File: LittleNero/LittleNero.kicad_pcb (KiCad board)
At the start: 2 copper layers, 24 parts, among them J1 USB_B_Mini, SW1 SW_push, U1 ATmega32U4-AU, Y1 16MHz

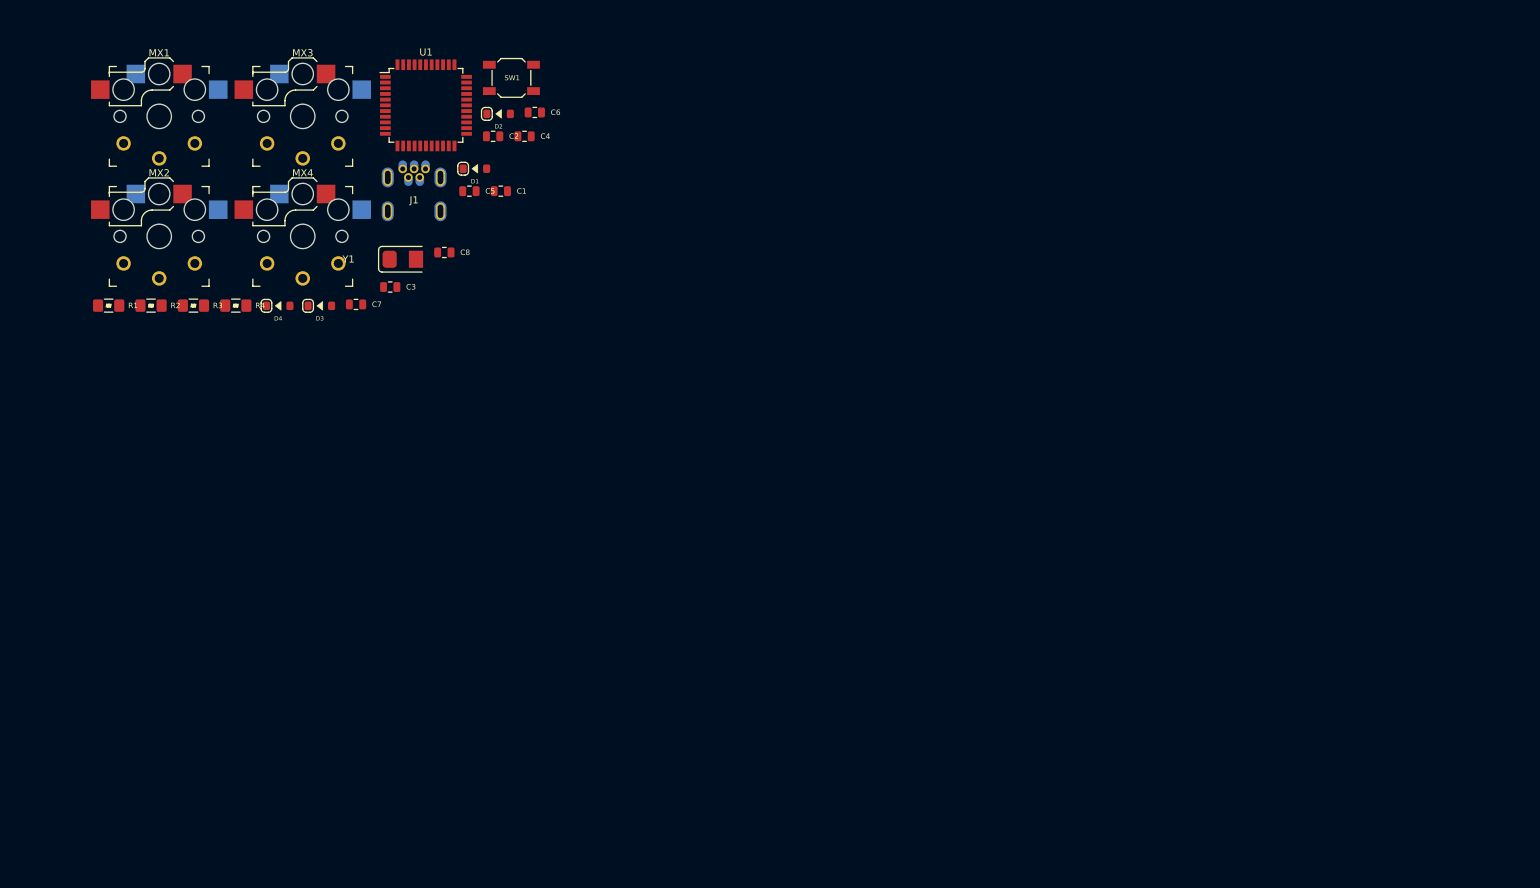
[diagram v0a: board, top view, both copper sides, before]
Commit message: updated schematic + visual pcb
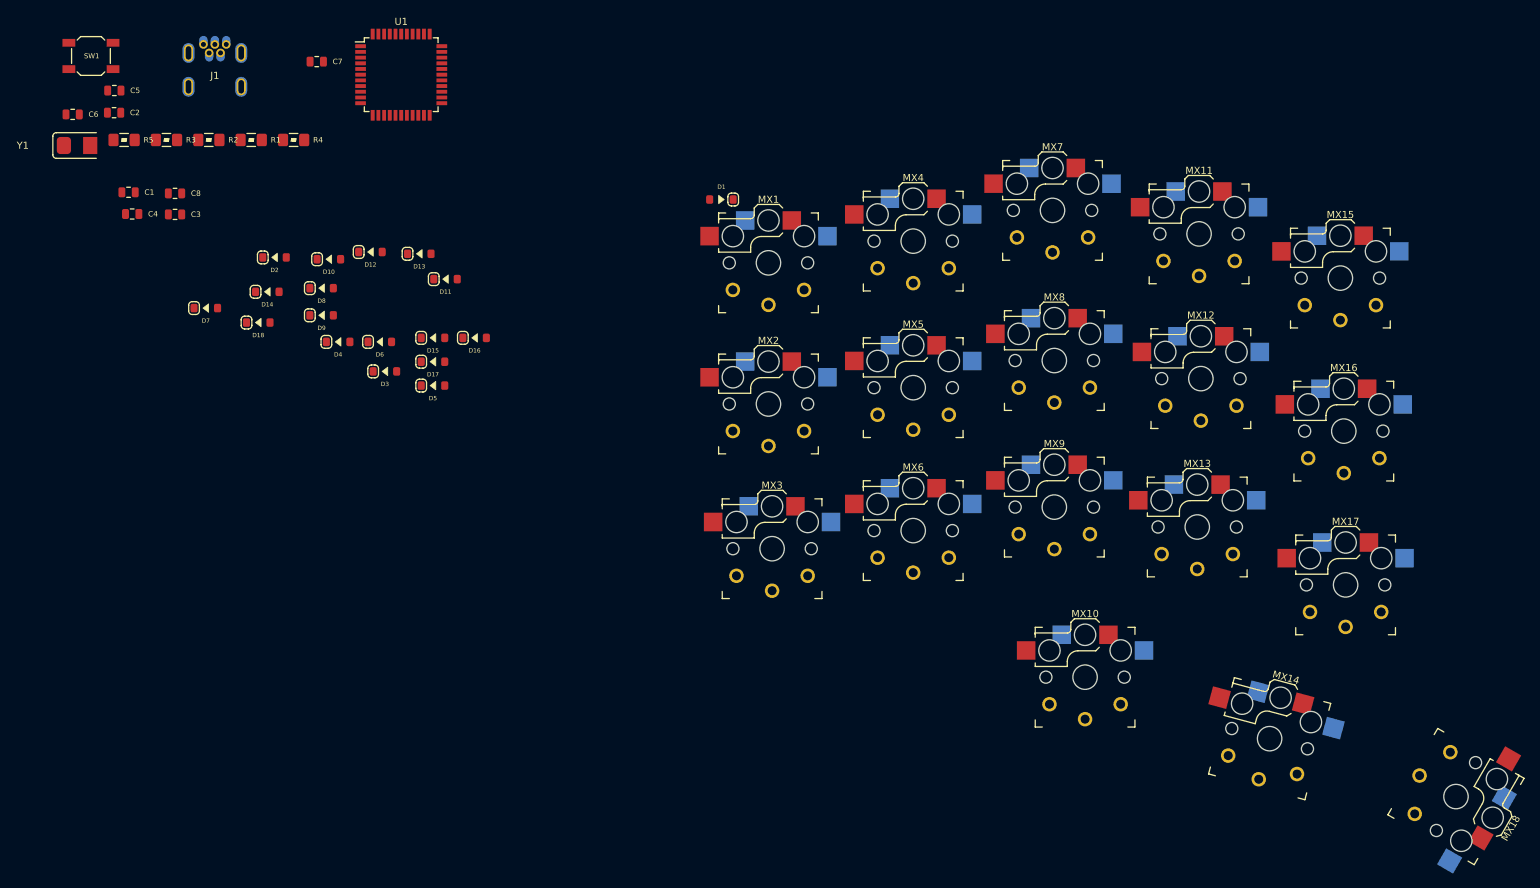
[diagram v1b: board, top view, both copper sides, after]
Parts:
- added D10: 1N4148W, acheron_Components:D_SOD-123, F.Cu at (51.8, 45.7)
- added D11: 1N4148W, acheron_Components:D_SOD-123, F.Cu at (68.2, 48.5)
- added D12: 1N4148W, acheron_Components:D_SOD-123, F.Cu at (57.7, 44.7)
- added D13: 1N4148W, acheron_Components:D_SOD-123, F.Cu at (64.5, 45.0)
- added D14: 1N4148W, acheron_Components:D_SOD-123, F.Cu at (43.2, 50.3)
- added D15: 1N4148W, acheron_Components:D_SOD-123, F.Cu at (66.4, 56.8)
- added D16: 1N4148W, acheron_Components:D_SOD-123, F.Cu at (72.3, 56.8)
- added D17: 1N4148W, acheron_Components:D_SOD-123, F.Cu at (66.4, 60.1)
- added D18: 1N4148W, acheron_Components:D_SOD-123, F.Cu at (41.9, 54.6)
- added D5: 1N4148W, acheron_Components:D_SOD-123, F.Cu at (66.4, 63.5)
- added D6: 1N4148W, acheron_Components:D_SOD-123, F.Cu at (59.0, 57.3)
- added D7: 1N4148W, acheron_Components:D_SOD-123, F.Cu at (34.5, 52.6)
- added D8: 1N4148W, acheron_Components:D_SOD-123, F.Cu at (50.8, 49.8)
- added D9: 1N4148W, acheron_Components:D_SOD-123, F.Cu at (50.8, 53.6)
- added MX10: mechSwitch, keyswitches:Kailh_socket_PG1350_optional_reversible, F.Cu at (158.0, 104.4)
- added MX11: mechSwitch, keyswitches:Kailh_socket_PG1350_optional_reversible, F.Cu at (174.0, 42.2)
- added MX12: mechSwitch, keyswitches:Kailh_socket_PG1350_optional_reversible, F.Cu at (174.2, 62.5)
- added MX13: mechSwitch, keyswitches:Kailh_socket_PG1350_optional_reversible, F.Cu at (173.7, 83.3)
- added MX14: mechSwitch, keyswitches:Kailh_socket_PG1350_optional_reversible_1.5, F.Cu at (183.9, 113.0)
- added MX15: mechSwitch, keyswitches:Kailh_socket_PG1350_optional_reversible, F.Cu at (193.8, 48.4)
- added MX16: mechSwitch, keyswitches:Kailh_socket_PG1350_optional_reversible, F.Cu at (194.3, 69.8)
- added MX17: mechSwitch, keyswitches:Kailh_socket_PG1350_optional_reversible, F.Cu at (194.6, 91.4)
- added MX18: mechSwitch, keyswitches:Kailh_socket_PG1350_optional_reversible_2, F.Cu at (210.1, 121.2)
- added MX5: mechSwitch, keyswitches:Kailh_socket_PG1350_optional_reversible, F.Cu at (133.9, 63.8)
- added MX6: mechSwitch, keyswitches:Kailh_socket_PG1350_optional_reversible, F.Cu at (133.9, 83.8)
- added MX7: mechSwitch, keyswitches:Kailh_socket_PG1350_optional_reversible, F.Cu at (153.4, 38.9)
- added MX8: mechSwitch, keyswitches:Kailh_socket_PG1350_optional_reversible, F.Cu at (153.7, 59.9)
- added MX9: mechSwitch, keyswitches:Kailh_socket_PG1350_optional_reversible, F.Cu at (153.7, 80.5)
- added R5: 1k, acheron_Components:R_SMD_1206, F.Cu at (23.1, 29.0)
- D1, D2, D3, D4: value D_Small -> 1N4148W
- R4: value 10k -> 330
- moved MX3 89.6 mm to (114.0, 86.4)
- moved MX2 88.7 mm to (113.5, 66.0)
- moved MX1 88.0 mm to (113.5, 46.2)
- moved MX4 85.7 mm to (133.9, 43.2)
- moved C6 64.9 mm to (15.9, 25.4)
- moved SW1 59.1 mm to (18.4, 17.2)
- moved C4 56.2 mm to (24.2, 39.4)
- moved C2 53.3 mm to (21.7, 25.1)
- moved C1 52.3 mm to (23.7, 36.3)
- moved C5 51.8 mm to (21.7, 22.0)
- moved Y1 48.4 mm to (16.5, 29.8)
- moved C8 38.7 mm to (30.2, 36.5)
- moved D2 37.4 mm to (44.2, 45.5)
- moved D1 34.9 mm to (106.9, 37.3), turned to 180 degrees
- moved C7 34.5 mm to (50.1, 18.0)
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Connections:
- net +5V renamed VCC
- C3 pad 1: GND -> Net-(C3-Pad1)
- D3 pad 1: Row1 -> Row3
- D4 pad 1: Row2 -> Row1
- MX3 pad 1: Col2 -> Col1
- R4 pad 2: Net-(R4-Pad2) -> Net-(C3-Pad1)
- SW1 pad 1: GND -> Net-(C3-Pad1)
- U1 pad 33: Net-(R4-Pad2) -> Net-(R5-Pad2)

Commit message: Add USB-C
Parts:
- added D19: PRTR5V0U2X_s, Package_TO_SOT_SMD:SOT-143_Handsoldering, F.Cu at (292.8, 149.4)
- added F1: 500mA, Fuse:Fuse_1206_3216Metric_Pad1.42x1.75mm_HandSolder, F.Cu at (301.6, 149.1)
- added J2: USB_C_Receptacle, Connector_USB:USB_C_Receptacle_Amphenol_12401548E4-2A, F.Cu at (122.8, 19.9)
- added J3: AudioJack4, Connector_Audio:Jack_3.5mm_PJ320D_Horizontal, F.Cu at (127.0, 39.6)
- added R6: 22, acheron_Components:R_SMD_1206, F.Cu at (315.5, 147.1)
- added R7: 22, acheron_Components:R_SMD_1206, F.Cu at (309.5, 153.7)
- C4: value 1u -> 1uF
- C6: value 1uF -> .1uF
- C7, C8: value 100nF -> .1uF
- MX1, MX10, MX11, MX12, MX13, MX15, MX16, MX17, MX2, MX3, MX4, MX5, MX6, MX7, MX8, MX9: footprint keyswitches:Kailh_socket_PG1350_optional_reversible -> keyswitches:Kailh_socket_PG1350_optional
- R1, R2: value 22 -> 5k
- R5: value 1k -> 10k
- SW1, U1: moved to B.Cu
- moved D18 315.4 mm to (332.7, 176.8)
- moved D14 311.1 mm to (332.5, 164.6)
- moved D7 310.7 mm to (331.7, 143.3)
- moved R2 310.6 mm to (319.7, 153.1)
- moved D10 300.0 mm to (332.2, 152.4)
- moved D2 299.1 mm to (331.5, 128.8)
- moved R1 299.0 mm to (317.5, 142.5)
- moved D8 297.3 mm to (332.0, 146.3)
- moved D12 297.2 mm to (332.2, 158.5)
- moved D9 297.0 mm to (332.0, 149.4)
- moved C1 292.7 mm to (301.6, 128.3)
- moved C2 292.7 mm to (299.5, 117.1)
- moved C6 292.7 mm to (293.7, 117.3)
- moved R3 292.7 mm to (306.9, 120.9)
- moved Y1 292.7 mm to (294.3, 121.7)
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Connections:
- C5 pad 2: VCC -> +5V
- C6 pad 2: VCC -> +5V
- C7 pad 2: VCC -> +5V
- C8 pad 2: VCC -> +5V
- J1 pad 1: VCC -> +5V
- J1 pad 2: Net-(J1-Pad2) -> D-
- J1 pad 3: Net-(J1-Pad3) -> D+
- R1 pad 1: D+ -> Net-(J2-PadA5)
- R1 pad 2: Net-(J1-Pad3) -> +5V
- R2 pad 1: D- -> Net-(J2-PadB5)
- R2 pad 2: Net-(J1-Pad2) -> +5V
- R3 pad 2: VCC -> +5V
- U1 pad 14: VCC -> +5V
- U1 pad 2: VCC -> +5V
- U1 pad 24: VCC -> +5V
- U1 pad 3: D- -> Net-(R7-Pad1)
- U1 pad 34: VCC -> +5V
- U1 pad 4: D+ -> Net-(R6-Pad1)
- U1 pad 44: VCC -> +5V
- U1 pad 7: VCC -> +5V
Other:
- board outline added: 129 x 111 mm
